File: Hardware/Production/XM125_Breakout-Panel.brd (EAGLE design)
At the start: 175 x 116.3 mm, 1266 parts, among them J104 SWD (DNP), J106 RIGHT_ANGLE, J107 RIGHT_ANGLE, J117 SWD (DNP), J119 RIGHT_ANGLE, J120 RIGHT_ANGLE, J13 SWD (DNP), J130 SWD (DNP), J132 RIGHT_ANGLE, J133 RIGHT_ANGLE, J143 SWD (DNP), J145 RIGHT_ANGLE, J146 RIGHT_ANGLE, J15 RIGHT_ANGLE, J156 SWD (DNP), J16 RIGHT_ANGLE, J2 RIGHT_ANGLE, J26 SWD (DNP), J28 RIGHT_ANGLE, J29 RIGHT_ANGLE, J3 RIGHT_ANGLE, J39 SWD (DNP), J41 RIGHT_ANGLE, J42 RIGHT_ANGLE, J52 SWD (DNP), J54 RIGHT_ANGLE, J55 RIGHT_ANGLE, J65 SWD (DNP), J67 RIGHT_ANGLE, J68 RIGHT_ANGLE, J78 SWD (DNP), J80 RIGHT_ANGLE, J81 RIGHT_ANGLE, J91 SWD (DNP), J93 RIGHT_ANGLE, J94 RIGHT_ANGLE, U1 XM125, U10 XM125, U11 CH340C, U12 ESD Diode, U13 RT9080-33GJ5, U14 RT9080-18GJ5, U15 XM125, U16 CH340C, U17 ESD Diode, U18 RT9080-33GJ5, U19 RT9080-18GJ5, U2 RT9080-33GJ5, U20 XM125, U21 CH340C, U22 ESD Diode, U23 RT9080-33GJ5, U24 RT9080-18GJ5, U25 XM125, U26 CH340C, U27 ESD Diode, U28 RT9080-33GJ5, U29 RT9080-18GJ5, U3 RT9080-18GJ5, U30 XM125, U31 CH340C, U32 ESD Diode, U33 RT9080-33GJ5, U34 RT9080-18GJ5, U35 XM125, U36 CH340C, U37 ESD Diode, U38 RT9080-33GJ5, U39 RT9080-18GJ5, U4 CH340C, U40 XM125, U41 CH340C, U42 ESD Diode, U43 RT9080-33GJ5, U44 RT9080-18GJ5, U45 XM125, U46 CH340C, U47 ESD Diode, U48 RT9080-33GJ5, U49 RT9080-18GJ5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

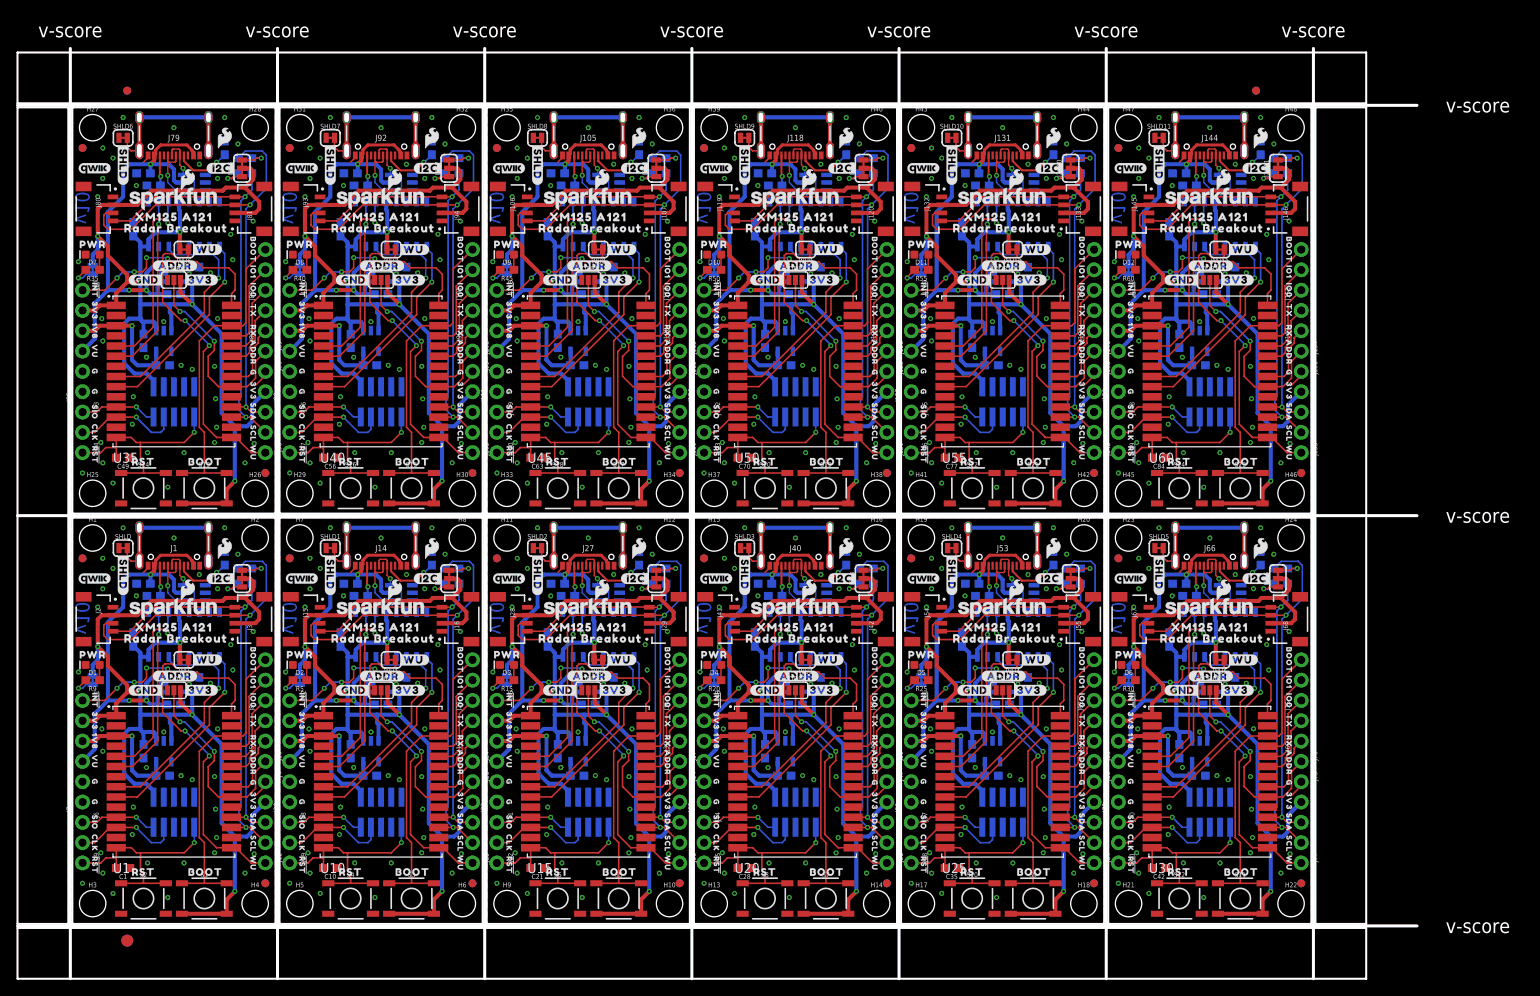
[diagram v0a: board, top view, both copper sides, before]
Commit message: Cleanup repo; design review changes
Check design review document for full list of changes/details.
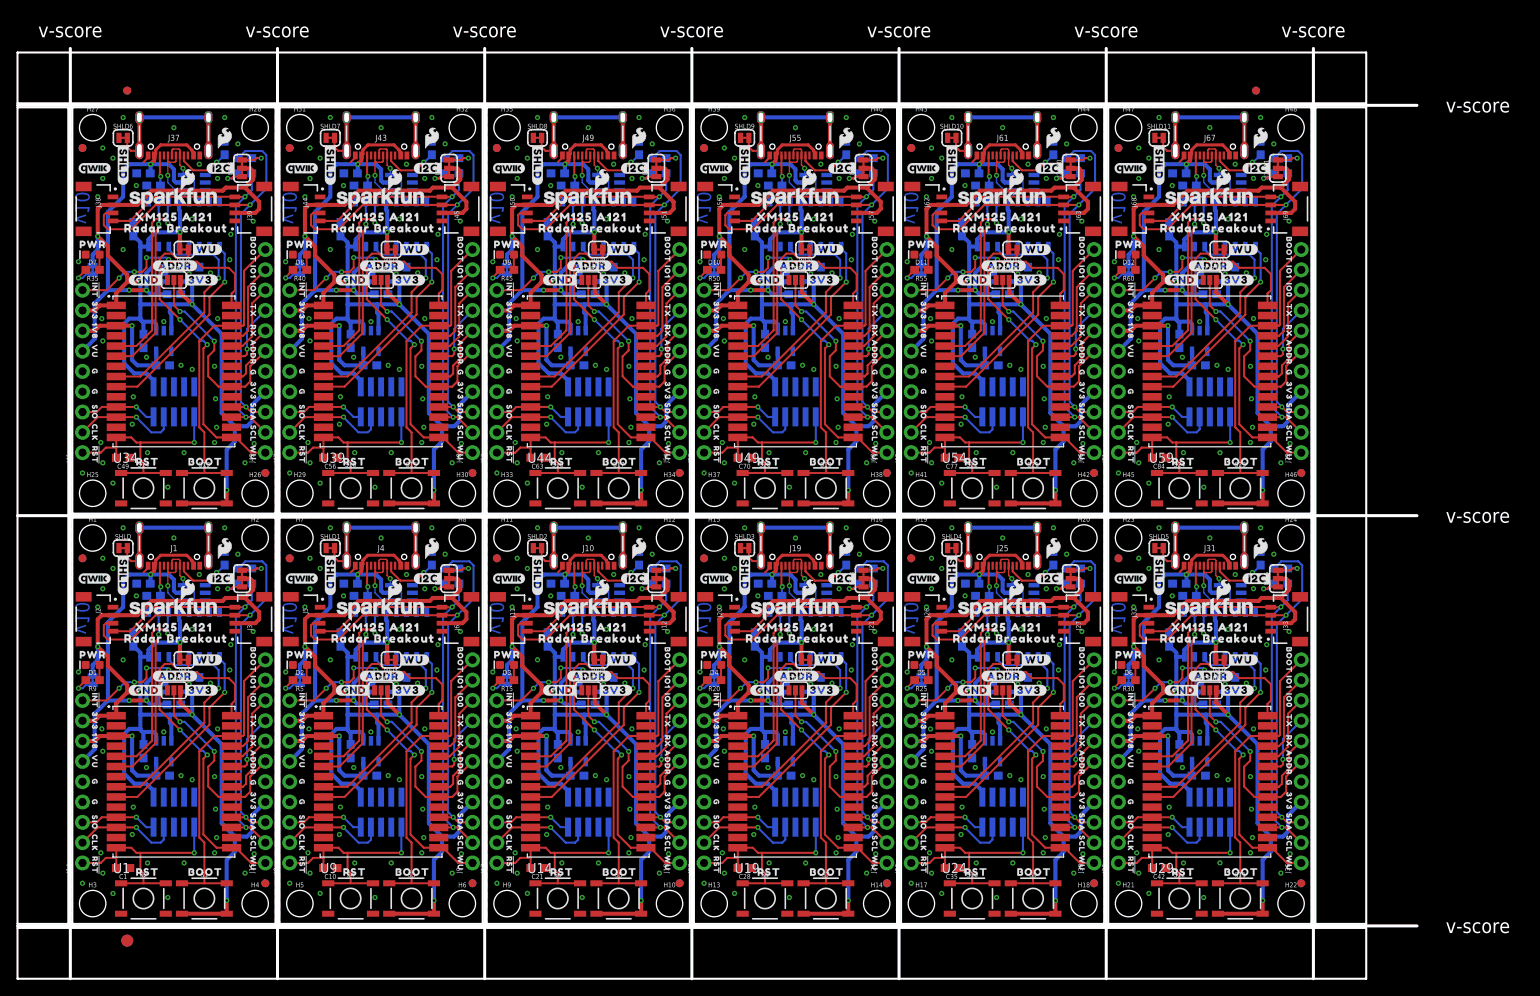
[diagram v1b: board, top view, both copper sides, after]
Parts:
- removed J100, J102, J103, J110, J113, J115, J116, J123, J126, J128, J129, J136, J139, J141, J142, J149, J152, J154, J155, J74, J76, J77, J84, J87, J89, J90, J97: (no value), SparkFun-Connectors:1X01_NO_SILK_STAND
- removed J101, J114, J127, J140, J153, J75, J88: (no value), SparkFun-Connectors:1X03_NO_SILK
- removed J104, J117, J130, J143, J156, J78, J91: SWD (DNP), SparkFun-Connectors:2X5-SMD-UNSHROUDED_DNP_NO_PASTE
- removed J105, J118, J131, J144, J79, J92: (no value), SparkFun-Connectors:USB-C-16P-2LAYER-PADS
- removed J106, J107, J119, J120, J132, J133, J145, J146, J80, J81, J93, J94: RIGHT_ANGLE, SparkFun-Connectors:JST04_1MM_RA
- removed J108, J109, J121, J122, J134, J135, J147, J148, J82, J83, J95, J96: (no value), SparkFun-Connectors:1X02_NO_SILK
- removed J111, J124, J137, J150, J85, J98: (no value), SparkFun-Connectors:1X05_NO_SILK
- removed J112, J125, J138, J151, J73, J86, J99: (no value), SparkFun-Connectors:1X04_NO_SILK
- J10, J19, J25, J37, J61: device SparkFun-Connectors:1X01_NO_SILK_STAND -> SparkFun-Connectors:USB-C-16P-2LAYER-PADS
- J11, J12, J32, J38, J45, J50, J51, J63: value (none) -> RIGHT_ANGLE; device SparkFun-Connectors:1X01_NO_SILK_STAND -> SparkFun-Connectors:JST04_1MM_RA
- J14, J53: device SparkFun-Connectors:USB-C-16P-2LAYER-PADS -> SparkFun-Connectors:1X09_NO_SILK
- J15, J42, J54: value RIGHT_ANGLE -> (none); device SparkFun-Connectors:JST04_1MM_RA -> SparkFun-Connectors:1X11_NO_SILK
- J16, J28: value RIGHT_ANGLE -> SWD (DNP); device SparkFun-Connectors:JST04_1MM_RA -> SparkFun-Connectors:2X5-SMD-UNSHROUDED_DNP_NO_PASTE
- J17: device SparkFun-Connectors:1X02_NO_SILK -> SparkFun-Connectors:1X09_NO_SILK
- J18, J30: device SparkFun-Connectors:1X02_NO_SILK -> SparkFun-Connectors:1X11_NO_SILK
- J20, J33: value (none) -> RIGHT_ANGLE; device SparkFun-Connectors:1X05_NO_SILK -> SparkFun-Connectors:JST04_1MM_RA
- J21: value (none) -> RIGHT_ANGLE; device SparkFun-Connectors:1X04_NO_SILK -> SparkFun-Connectors:JST04_1MM_RA
- J22, J58, J64: value (none) -> SWD (DNP); device SparkFun-Connectors:1X01_NO_SILK_STAND -> SparkFun-Connectors:2X5-SMD-UNSHROUDED_DNP_NO_PASTE
- J23, J8: device SparkFun-Connectors:1X03_NO_SILK -> SparkFun-Connectors:1X09_NO_SILK
- J24, J48, J9: device SparkFun-Connectors:1X01_NO_SILK_STAND -> SparkFun-Connectors:1X11_NO_SILK
- J26, J39: value SWD (DNP) -> RIGHT_ANGLE; device SparkFun-Connectors:2X5-SMD-UNSHROUDED_DNP_NO_PASTE -> SparkFun-Connectors:JST04_1MM_RA
- J27: value (none) -> RIGHT_ANGLE; device SparkFun-Connectors:USB-C-16P-2LAYER-PADS -> SparkFun-Connectors:JST04_1MM_RA
- J29, J41: value RIGHT_ANGLE -> (none); device SparkFun-Connectors:JST04_1MM_RA -> SparkFun-Connectors:1X09_NO_SILK
- J31, J43: device SparkFun-Connectors:1X02_NO_SILK -> SparkFun-Connectors:USB-C-16P-2LAYER-PADS
- J34: value (none) -> SWD (DNP); device SparkFun-Connectors:1X04_NO_SILK -> SparkFun-Connectors:2X5-SMD-UNSHROUDED_DNP_NO_PASTE
- J35, J71: device SparkFun-Connectors:1X01_NO_SILK_STAND -> SparkFun-Connectors:1X09_NO_SILK
- J36: device SparkFun-Connectors:1X03_NO_SILK -> SparkFun-Connectors:1X11_NO_SILK
- J4: device SparkFun-Connectors:1X04_NO_SILK -> SparkFun-Connectors:USB-C-16P-2LAYER-PADS
- J40: value (none) -> SWD (DNP); device SparkFun-Connectors:USB-C-16P-2LAYER-PADS -> SparkFun-Connectors:2X5-SMD-UNSHROUDED_DNP_NO_PASTE
- J44, J5, J56, J57, J6, J69: value (none) -> RIGHT_ANGLE; device SparkFun-Connectors:1X02_NO_SILK -> SparkFun-Connectors:JST04_1MM_RA
- J46, J7: value (none) -> SWD (DNP); device SparkFun-Connectors:1X05_NO_SILK -> SparkFun-Connectors:2X5-SMD-UNSHROUDED_DNP_NO_PASTE
- J47: device SparkFun-Connectors:1X04_NO_SILK -> SparkFun-Connectors:1X09_NO_SILK
- J49: device SparkFun-Connectors:1X03_NO_SILK -> SparkFun-Connectors:USB-C-16P-2LAYER-PADS
- J55, J67: value RIGHT_ANGLE -> (none); device SparkFun-Connectors:JST04_1MM_RA -> SparkFun-Connectors:USB-C-16P-2LAYER-PADS
- J59: device SparkFun-Connectors:1X05_NO_SILK -> SparkFun-Connectors:1X09_NO_SILK
- J60: device SparkFun-Connectors:1X04_NO_SILK -> SparkFun-Connectors:1X11_NO_SILK
- J62: value (none) -> RIGHT_ANGLE; device SparkFun-Connectors:1X03_NO_SILK -> SparkFun-Connectors:JST04_1MM_RA
- J65: value SWD (DNP) -> (none); device SparkFun-Connectors:2X5-SMD-UNSHROUDED_DNP_NO_PASTE -> SparkFun-Connectors:1X09_NO_SILK
- J66: device SparkFun-Connectors:USB-C-16P-2LAYER-PADS -> SparkFun-Connectors:1X11_NO_SILK
- J70: value (none) -> SWD (DNP); device SparkFun-Connectors:1X02_NO_SILK -> SparkFun-Connectors:2X5-SMD-UNSHROUDED_DNP_NO_PASTE
- J72: device SparkFun-Connectors:1X05_NO_SILK -> SparkFun-Connectors:1X11_NO_SILK
- U10, U15, U20, U25, U30, U35, U40, U45, U50, U55, U60: value XM125 -> ESD Diode; device XM125:XM125_ACC -> SparkFun-DiscreteSemi:SOT-23-6
- U12, U17, U22, U27, U32, U37, U42, U47, U52, U57, U7: value ESD Diode -> RT9080-33GJ5; device SparkFun-DiscreteSemi:SOT-23-6 -> SparkFun-IC-Power:SOT23-5
- U13, U18, U23, U28, U33, U38, U43, U48, U53, U58, U8: value RT9080-33GJ5 -> RT9080-18GJ5; device SparkFun-IC-Power:SOT23-5 -> XM125:SOT23-5
- U14, U19, U24, U29, U34, U39, U44, U49, U54, U59, U9: value RT9080-18GJ5 -> XM125; device XM125:SOT23-5 -> XM125:XM125_ACC
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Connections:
- removed net N$100: J144.A6, J144.B6, U56.5, U57.4
- removed net N$19 (its old number): J27.A6, J27.B6, U11.5, U12.4
- removed net N$20: J27.A7, J27.B7, U11.6, U12.6
- removed net N$28 (its old number): J40.A6, J40.B6, U16.5, U17.4
- removed net N$29 (its old number): J40.A7, J40.B7, U16.6, U17.6
- removed net N$3: J14.A6, J14.B6, U6.5, U7.4
- removed net N$30: J40.SHLD1, J40.SHLD2, J40.SHLD3, J40.SHLD4, SHLD3.2
- removed net N$37 (its old number): J53.A6, J53.B6, U21.5, U22.4
- removed net N$38 (its old number): J53.A7, J53.B7, U21.6, U22.6
- removed net N$39 (its old number): J53.SHLD1, J53.SHLD2, J53.SHLD3, J53.SHLD4, SHLD4.2
- removed net N$40: J53.B5, R22.2
- removed net N$46 (its old number): J66.A6, J66.B6, U26.5, U27.4
- removed net N$47 (its old number): J66.A7, J66.B7, U26.6, U27.6
- removed net N$48 (its old number): J66.SHLD1, J66.SHLD2, J66.SHLD3, J66.SHLD4, SHLD5.2
- removed net N$49 (its old number): J66.B5, R27.2
- removed net N$50: J66.A5, R26.2
- removed net N$56 (its old number): J79.A7, J79.B7, U31.6, U32.6
- removed net N$57 (its old number): J79.SHLD1, J79.SHLD2, J79.SHLD3, J79.SHLD4, SHLD6.2
- removed net N$58 (its old number): J79.B5, R32.2
- removed net N$59 (its old number): J79.A5, R31.2
- removed net N$66 (its old number): J92.SHLD1, J92.SHLD2, J92.SHLD3, J92.SHLD4, SHLD7.2
- removed net N$67 (its old number): J92.B5, R37.2
- removed net N$68 (its old number): J92.A5, R36.2
- removed net N$76 (its old number): J105.B5, R42.2
- removed net N$77 (its old number): J105.A5, R41.2
- removed net N$86 (its old number): J118.A5, R46.2
- new net N$105: J61.A5, R51.2
- new net N$111: J67.A6, J67.B6, U56.5, U60.4
- new net N$112: J67.A7, J67.B7, U56.6, U60.6
- new net N$113: J67.SHLD1, J67.SHLD2, J67.SHLD3, J67.SHLD4, SHLD11.2
- new net N$114: J67.B5, R57.2
- new net N$115: J67.A5, R56.2
- new net N$24: J10.B5, R10.2
- new net N$25: J10.A5, R6.2
- new net N$33: J19.SHLD1, J19.SHLD2, J19.SHLD3, J19.SHLD4, SHLD3.2
- new net N$34: J19.B5, R17.2
- new net N$35: J19.A5, R16.2
- new net N$42: J25.A7, J25.B7, U21.6, U25.6
- new net N$43: J25.SHLD1, J25.SHLD2, J25.SHLD3, J25.SHLD4, SHLD4.2
- new net N$44: J25.B5, R22.2
- new net N$45: J25.A5, R21.2
- new net N$51: J31.A6, J31.B6, U26.5, U30.4
- new net N$52: J31.A7, J31.B7, U26.6, U30.6
- new net N$53: J31.SHLD1, J31.SHLD2, J31.SHLD3, J31.SHLD4, SHLD5.2
- new net N$54: J31.B5, R27.2
- new net N$61: J37.A6, J37.B6, U31.5, U35.4
- new net N$62: J37.A7, J37.B7, U31.6, U35.6
- new net N$63: J37.SHLD1, J37.SHLD2, J37.SHLD3, J37.SHLD4, SHLD6.2
- new net N$71: J43.A6, J43.B6, U36.5, U40.4
- new net N$72: J43.A7, J43.B7, U36.6, U40.6
- new net N$8: J4.A5, R1.2
- new net N$81: J49.A6, J49.B6, U41.5, U45.4
- net !XM125_INT: now also J14.9; no longer J11.1
- net !XM125_INT1: now also J8.9, U9.28; no longer J22.1, U10.28
- net !XM125_INT10: now also J65.9, U54.28; no longer J139.1, U55.28
- net !XM125_INT11: now also J71.9, U59.28; no longer J152.1, U60.28
- net !XM125_INT2: now also J17.9, U14.28; no longer J35.1, U15.28
- net !XM125_INT3: now also J23.9, U19.28; no longer J48.1, U20.28
- net !XM125_INT4: now also J29.9, U24.28; no longer J61.1, U25.28
- net !XM125_INT5: now also J35.9, U29.28; no longer J74.1, U30.28
- net !XM125_INT6: now also J41.9, U34.28; no longer J87.1, U35.28
- net !XM125_INT7: now also J47.9, U39.28; no longer J100.1, U40.28
- net !XM125_INT8: now also J53.9, U44.28; no longer J113.1, U45.28
- net !XM125_INT9: now also J59.9, U49.28; no longer J126.1, U50.28
- net !XM125_RESET: now also J14.1; no longer J9.1
- net !XM125_RESET1: now also J7.10, J8.1, U9.14; no longer J19.1, J26.10, U10.14
- net !XM125_RESET10: now also J64.10, J65.1, U54.14; no longer J136.1, J143.10, U55.14
- net !XM125_RESET11: now also J70.10, J71.1, U59.14; no longer J149.1, J156.10, U60.14
- net !XM125_RESET2: now also J16.10, J17.1, U14.14; no longer J32.1, J39.10, U15.14
- net !XM125_RESET3: now also J22.10, J23.1, U19.14; no longer J45.1, J52.10, U20.14
- net !XM125_RESET4: now also J28.10, J29.1, U24.14; no longer J58.1, J65.10, U25.14
- net !XM125_RESET5: now also J34.10, J35.1, U29.14; no longer J71.1, J78.10, U30.14
- net !XM125_RESET6: now also J40.10, J41.1, U34.14; no longer J84.1, J91.10, U35.14
- net !XM125_RESET7: now also J46.10, J47.1, U39.14; no longer J104.10, J97.1, U40.14
- net !XM125_RESET8: now also J52.10, J53.1, U44.14; no longer J110.1, J117.10, U45.14
- net !XM125_RESET9: now also J58.10, J59.1, U49.14; no longer J123.1, J130.10, U50.14
- net 1.8V: now also J14.7; no longer J7.4
- net 1.8V1: now also J8.7, U8.5, U9.3; no longer J20.4, U10.3, U9.5
- net 1.8V10: now also J65.7, U53.5, U54.3; no longer J137.4, U54.5, U55.3
- net 1.8V11: now also J71.7, U58.5, U59.3; no longer J150.4, U59.5, U60.3
- net 1.8V2: now also J17.7, U13.5, U14.3; no longer J33.4, U14.5, U15.3
- net 1.8V3: now also J23.7, U18.5, U19.3; no longer J46.4, U19.5, U20.3
- net 1.8V4: now also J29.7, U23.5, U24.3; no longer J59.4, U24.5, U25.3
- net 1.8V5: now also J35.7, U28.5, U29.3; no longer J72.4, U29.5, U30.3
- net 1.8V6: now also J41.7, U33.5, U34.3; no longer J85.4, U34.5, U35.3
- net 1.8V7: now also J47.7, U38.5, U39.3; no longer J98.4, U39.5, U40.3
- net 1.8V8: now also J53.7, U43.5, U44.3; no longer J111.4, U44.5, U45.3
- net 1.8V9: now also J59.7, U48.5, U49.3; no longer J124.4, U49.5, U50.3
- net 3.3V: now also J14.8, J15.4; no longer J4.2, J7.5
- net 3.3V1: now also J5.2, J6.2, J7.1, J8.8, J9.4, U7.5, U8.1, U8.3; no longer J15.2, J16.2, J20.5, J21.2, J26.1, U10.1, U8.5, U9.3
- net 3.3V10: now also J62.2, J63.2, J64.1, J65.8, J66.4, U52.5, U53.1, U53.3; no longer J132.2, J133.2, J137.5, J138.2, J143.1, U53.5, U54.3, U55.1
- net 3.3V11: now also J68.2, J69.2, J70.1, J71.8, J72.4, U57.5, U58.1, U58.3; no longer J145.2, J146.2, J150.5, J151.2, J156.1, U58.5, U59.3, U60.1
- net 3.3V2: now also J11.2, J12.2, J16.1, J17.8, J18.4, U12.5, U13.1, U13.3; no longer J28.2, J29.2, J33.5, J34.2, J39.1, U13.5, U14.3, U15.1
- net 3.3V3: now also J20.2, J21.2, J22.1, J23.8, J24.4, U17.5, U18.1, U18.3; no longer J41.2, J42.2, J46.5, J47.2, J52.1, U18.5, U19.3, U20.1
- net 3.3V4: now also J26.2, J27.2, J28.1, J29.8, J30.4, U22.5, U23.1, U23.3; no longer J54.2, J55.2, J59.5, J60.2, J65.1, U23.5, U24.3, U25.1
- net 3.3V5: now also J32.2, J33.2, J34.1, J35.8, J36.4, U27.5, U28.1, U28.3; no longer J67.2, J68.2, J72.5, J73.2, J78.1, U28.5, U29.3, U30.1
- net 3.3V6: now also J38.2, J39.2, J40.1, J41.8, J42.4, U32.5, U33.1, U33.3; no longer J80.2, J81.2, J85.5, J86.2, J91.1, U33.5, U34.3, U35.1
- net 3.3V7: now also J44.2, J45.2, J46.1, J47.8, J48.4, U37.5, U38.1, U38.3; no longer J104.1, J93.2, J94.2, J98.5, J99.2, U38.5, U39.3, U40.1
- net 3.3V8: now also J50.2, J51.2, J52.1, J53.8, J54.4, U42.5, U43.1, U43.3; no longer J106.2, J107.2, J111.5, J112.2, J117.1, U43.5, U44.3, U45.1
- net 3.3V9: now also J56.2, J57.2, J58.1, J59.8, J60.4, U47.5, U48.1, U48.3; no longer J119.2, J120.2, J124.5, J125.2, J130.1, U48.5, U49.3, U50.1
- net CH340-CTS1: now also U9.9; no longer U10.9
- net CH340-CTS10: now also U54.9; no longer U55.9
- net CH340-CTS11: now also U59.9; no longer U60.9
- net CH340-CTS2: now also U14.9; no longer U15.9
- net CH340-CTS3: now also U19.9; no longer U20.9
- net CH340-CTS4: now also U24.9; no longer U25.9
- net CH340-CTS5: now also U29.9; no longer U30.9
- net CH340-CTS6: now also U34.9; no longer U35.9
- net CH340-CTS7: now also U39.9; no longer U40.9
- net CH340-CTS8: now also U44.9; no longer U45.9
- net CH340-CTS9: now also U49.9; no longer U50.9
- net CH340-RTS1: now also U9.8; no longer U10.8
- net CH340-RTS10: now also U54.8; no longer U55.8
- net CH340-RTS11: now also U59.8; no longer U60.8
- net CH340-RTS2: now also U14.8; no longer U15.8
- net CH340-RTS3: now also U19.8; no longer U20.8
- net CH340-RTS4: now also U24.8; no longer U25.8
- net CH340-RTS5: now also U29.8; no longer U30.8
- net CH340-RTS6: now also U34.8; no longer U35.8
- net CH340-RTS7: now also U39.8; no longer U40.8
- net CH340-RTS8: now also U44.8; no longer U45.8
- net CH340-RTS9: now also U49.8; no longer U50.8
- net CH340-RX1: now also U9.5; no longer U10.5
- net CH340-RX10: now also U54.5; no longer U55.5
- net CH340-RX11: now also U59.5; no longer U60.5
- net CH340-RX2: now also U14.5; no longer U15.5
- net CH340-RX3: now also U19.5; no longer U20.5
- net CH340-RX4: now also U24.5; no longer U25.5
- net CH340-RX5: now also U29.5; no longer U30.5
- net CH340-RX6: now also U34.5; no longer U35.5
- net CH340-RX7: now also U39.5; no longer U40.5
- net CH340-RX8: now also U44.5; no longer U45.5
- net CH340-RX9: now also U49.5; no longer U50.5
- net CH340-TX1: now also U9.6; no longer U10.6
- net CH340-TX10: now also U54.6; no longer U55.6
- net CH340-TX11: now also U59.6; no longer U60.6
- net CH340-TX2: now also U14.6; no longer U15.6
- net CH340-TX3: now also U19.6; no longer U20.6
- net CH340-TX4: now also U24.6; no longer U25.6
- net CH340-TX5: now also U29.6; no longer U30.6
- net CH340-TX6: now also U34.6; no longer U35.6
- net CH340-TX7: now also U39.6; no longer U40.6
- net CH340-TX8: now also U44.6; no longer U45.6
- net CH340-TX9: now also U49.6; no longer U50.6
- net DEBUG_UART-RX: now also J15.7; no longer J5.1
- net DEBUG_UART-RX1: now also J9.7, U9.21; no longer J17.1, U10.21
- net DEBUG_UART-RX10: now also J66.7, U54.21; no longer J134.1, U55.21
- net DEBUG_UART-RX11: now also J72.7, U59.21; no longer J147.1, U60.21
- net DEBUG_UART-RX2: now also J18.7, U14.21; no longer J30.1, U15.21
- net DEBUG_UART-RX3: now also J24.7, U19.21; no longer J43.1, U20.21
- net DEBUG_UART-RX4: now also J30.7, U24.21; no longer J56.1, U25.21
- net DEBUG_UART-RX5: now also J36.7, U29.21; no longer J69.1, U30.21
- net DEBUG_UART-RX6: now also J42.7, U34.21; no longer J82.1, U35.21
- net DEBUG_UART-RX7: now also J48.7, U39.21; no longer J95.1, U40.21
- net DEBUG_UART-RX8: now also J54.7, U44.21; no longer J108.1, U45.21
- net DEBUG_UART-RX9: now also J60.7, U49.21; no longer J121.1, U50.21
- net DEBUG_UART-TX: now also J15.8; no longer J5.2
- net DEBUG_UART-TX1: now also J9.8, U9.23; no longer J17.2, U10.23
- net DEBUG_UART-TX10: now also J66.8, U54.23; no longer J134.2, U55.23
- net DEBUG_UART-TX11: now also J72.8, U59.23; no longer J147.2, U60.23
- net DEBUG_UART-TX2: now also J18.8, U14.23; no longer J30.2, U15.23
- net DEBUG_UART-TX3: now also J24.8, U19.23; no longer J43.2, U20.23
- net DEBUG_UART-TX4: now also J30.8, U24.23; no longer J56.2, U25.23
- net DEBUG_UART-TX5: now also J36.8, U29.23; no longer J69.2, U30.23
- net DEBUG_UART-TX6: now also J42.8, U34.23; no longer J82.2, U35.23
- net DEBUG_UART-TX7: now also J48.8, U39.23; no longer J95.2, U40.23
- net DEBUG_UART-TX8: now also J54.8, U44.23; no longer J108.2, U45.23
- net DEBUG_UART-TX9: now also J60.8, U49.23; no longer J121.2, U50.23
- net GND: now also J14.4, J14.5, J15.5; no longer J4.1, J7.1, J7.2
- net GND1: now also J4.GND, J4.GND2, J5.1, J6.1, J7.3, J7.5, J7.9, J8.4, J8.5, J9.5, U9.10, U9.13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; no longer J14.GND, J14.GND2, J15.1, J16.1, J20.1, J20.2, J21.1, J26.3, J26.5, J26.9, U10.10, U10.13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
- net GND10: now also J61.GND, J61.GND2, J62.1, J63.1, J64.3, J64.5, J64.9, J65.4, J65.5, J66.5, U54.10, U54.13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; no longer J131.GND, J131.GND2, J132.1, J133.1, J137.1, J137.2, J138.1, J143.3, J143.5, J143.9, U55.10, U55.13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
- net GND11: now also J67.GND, J67.GND2, J68.1, J69.1, J70.3, J70.5, J70.9, J71.4, J71.5, J72.5, U59.10, U59.13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; no longer J144.GND, J144.GND2, J145.1, J146.1, J150.1, J150.2, J151.1, J156.3, J156.5, J156.9, U60.10, U60.13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
- net GND2: now also J10.GND, J10.GND2, J11.1, J12.1, J16.3, J16.5, J16.9, J17.4, J17.5, J18.5, U14.10, U14.13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; no longer J27.GND, J27.GND2, J28.1, J29.1, J33.1, J33.2, J34.1, J39.3, J39.5, J39.9, U15.10, U15.13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
- net GND3: now also J19.GND, J19.GND2, J20.1, J21.1, J22.3, J22.5, J22.9, J23.4, J23.5, J24.5, U19.10, U19.13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; no longer J40.GND, J40.GND2, J41.1, J42.1, J46.1, J46.2, J47.1, J52.3, J52.5, J52.9, U20.10, U20.13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
- net GND4: now also J25.GND, J25.GND2, J26.1, J27.1, J28.3, J28.5, J28.9, J29.4, J29.5, J30.5, U24.10, U24.13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; no longer J53.GND, J53.GND2, J54.1, J55.1, J59.1, J59.2, J60.1, J65.3, J65.5, J65.9, U25.10, U25.13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
- net GND5: now also J31.GND, J31.GND2, J32.1, J33.1, J34.3, J34.5, J34.9, J35.4, J35.5, J36.5, U29.10, U29.13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; no longer J66.GND, J66.GND2, J67.1, J68.1, J72.1, J72.2, J73.1, J78.3, J78.5, J78.9, U30.10, U30.13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
- net GND6: now also J37.GND, J37.GND2, J38.1, J39.1, J40.3, J40.5, J40.9, J41.4, J41.5, J42.5, U34.10, U34.13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; no longer J79.GND, J79.GND2, J80.1, J81.1, J85.1, J85.2, J86.1, J91.3, J91.5, J91.9, U35.10, U35.13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
- net GND7: now also J43.GND, J43.GND2, J44.1, J45.1, J46.3, J46.5, J46.9, J47.4, J47.5, J48.5, U39.10, U39.13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; no longer J104.3, J104.5, J104.9, J92.GND, J92.GND2, J93.1, J94.1, J98.1, J98.2, J99.1, U40.10, U40.13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
- net GND8: now also J49.GND, J49.GND2, J50.1, J51.1, J52.3, J52.5, J52.9, J53.4, J53.5, J54.5, U44.10, U44.13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; no longer J105.GND, J105.GND2, J106.1, J107.1, J111.1, J111.2, J112.1, J117.3, J117.5, J117.9, U45.10, U45.13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
- net GND9: now also J55.GND, J55.GND2, J56.1, J57.1, J58.3, J58.5, J58.9, J59.4, J59.5, J60.5, U49.10, U49.13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; no longer J118.GND, J118.GND2, J119.1, J120.1, J124.1, J124.2, J125.1, J130.3, J130.5, J130.9, U50.10, U50.13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
- net N$101: now also J61.A6, J61.B6, U51.5, U55.4; no longer J144.A7, J144.B7, U56.6, U57.6
- net N$102: now also J61.A7, J61.B7, U51.6, U55.6; no longer J144.SHLD1, J144.SHLD2, J144.SHLD3, J144.SHLD4, SHLD11.2
- net N$103: now also J61.SHLD1, J61.SHLD2, J61.SHLD3, J61.SHLD4, SHLD10.2; no longer J144.B5, R57.2
- net N$104: now also J61.B5, R52.2; no longer J144.A5, R56.2
- net N$21: now also J10.A6, J10.B6, U11.5, U15.4; no longer J27.SHLD1, J27.SHLD2, J27.SHLD3, J27.SHLD4, SHLD2.2
- net N$22: now also J10.A7, J10.B7, U11.6, U15.6; no longer J27.B5, R10.2
- net N$23: now also J10.SHLD1, J10.SHLD2, J10.SHLD3, J10.SHLD4, SHLD2.2; no longer J27.A5, R6.2
- net N$31: now also J19.A6, J19.B6, U16.5, U20.4; no longer J40.B5, R17.2
- net N$32: now also J19.A7, J19.B7, U16.6, U20.6; no longer J40.A5, R16.2
- net N$4: now also J4.A6, J4.B6, U10.4, U6.5; no longer J14.A7, J14.B7, U6.6, U7.6
- net N$41: now also J25.A6, J25.B6, U21.5, U25.4; no longer J53.A5, R21.2
- net N$5: now also J4.A7, J4.B7, U10.6, U6.6; no longer J14.SHLD1, J14.SHLD2, J14.SHLD3, J14.SHLD4, SHLD1.2
- net N$55: now also J31.A5, R26.2; no longer J79.A6, J79.B6, U31.5, U32.4
- net N$6: now also J4.SHLD1, J4.SHLD2, J4.SHLD3, J4.SHLD4, SHLD1.2; no longer J14.B5, R2.2
- net N$64: now also J37.B5, R32.2; no longer J92.A6, J92.B6, U36.5, U37.4
- net N$65: now also J37.A5, R31.2; no longer J92.A7, J92.B7, U36.6, U37.6
- net N$7: now also J4.B5, R2.2; no longer J14.A5, R1.2
- net N$73: now also J43.SHLD1, J43.SHLD2, J43.SHLD3, J43.SHLD4, SHLD7.2; no longer J105.A6, J105.B6, U41.5, U42.4
- net N$74: now also J43.B5, R37.2; no longer J105.A7, J105.B7, U41.6, U42.6
- net N$75: now also J43.A5, R36.2; no longer J105.SHLD1, J105.SHLD2, J105.SHLD3, J105.SHLD4, SHLD8.2
- net N$82: now also J49.A7, J49.B7, U41.6, U45.6; no longer J118.A6, J118.B6, U46.5, U47.4
- net N$83: now also J49.SHLD1, J49.SHLD2, J49.SHLD3, J49.SHLD4, SHLD8.2; no longer J118.A7, J118.B7, U46.6, U47.6
- net N$84: now also J49.B5, R42.2; no longer J118.SHLD1, J118.SHLD2, J118.SHLD3, J118.SHLD4, SHLD9.2
- net N$85: now also J49.A5, R41.2; no longer J118.B5, R47.2
- net N$91: now also J55.A6, J55.B6, U46.5, U50.4; no longer J131.A6, J131.B6, U51.5, U52.4
- net N$92: now also J55.A7, J55.B7, U46.6, U50.6; no longer J131.A7, J131.B7, U51.6, U52.6
- net N$93: now also J55.SHLD1, J55.SHLD2, J55.SHLD3, J55.SHLD4, SHLD9.2; no longer J131.SHLD1, J131.SHLD2, J131.SHLD3, J131.SHLD4, SHLD10.2
- net N$94: now also J55.B5, R47.2; no longer J131.B5, R52.2
- net N$95: now also J55.A5, R46.2; no longer J131.A5, R51.2
- net SCL: now also J15.2; no longer J4.4
- net SCL1: now also J5.4, J6.4, J9.2, U9.17; no longer J15.4, J16.4, J21.4, U10.17
- net SCL10: now also J62.4, J63.4, J66.2, U54.17; no longer J132.4, J133.4, J138.4, U55.17
- net SCL11: now also J68.4, J69.4, J72.2, U59.17; no longer J145.4, J146.4, J151.4, U60.17
- net SCL2: now also J11.4, J12.4, J18.2, U14.17; no longer J28.4, J29.4, J34.4, U15.17
- net SCL3: now also J20.4, J21.4, J24.2, U19.17; no longer J41.4, J42.4, J47.4, U20.17
- net SCL4: now also J26.4, J27.4, J30.2, U24.17; no longer J54.4, J55.4, J60.4, U25.17
- net SCL5: now also J32.4, J33.4, J36.2, U29.17; no longer J67.4, J68.4, J73.4, U30.17
- net SCL6: now also J38.4, J39.4, J42.2, U34.17; no longer J80.4, J81.4, J86.4, U35.17
- net SCL7: now also J44.4, J45.4, J48.2, U39.17; no longer J93.4, J94.4, J99.4, U40.17
- net SCL8: now also J50.4, J51.4, J54.2, U44.17; no longer J106.4, J107.4, J112.4, U45.17
- net SCL9: now also J56.4, J57.4, J60.2, U49.17; no longer J119.4, J120.4, J125.4, U50.17
- net SDA: now also J15.3; no longer J4.3
- net SDA1: now also J5.3, J6.3, J9.3, U9.18; no longer J15.3, J16.3, J21.3, U10.18
- net SDA10: now also J62.3, J63.3, J66.3, U54.18; no longer J132.3, J133.3, J138.3, U55.18
- net SDA11: now also J68.3, J69.3, J72.3, U59.18; no longer J145.3, J146.3, J151.3, U60.18
- net SDA2: now also J11.3, J12.3, J18.3, U14.18; no longer J28.3, J29.3, J34.3, U15.18
- net SDA3: now also J20.3, J21.3, J24.3, U19.18; no longer J41.3, J42.3, J47.3, U20.18
- net SDA4: now also J26.3, J27.3, J30.3, U24.18; no longer J54.3, J55.3, J60.3, U25.18
- net SDA5: now also J32.3, J33.3, J36.3, U29.18; no longer J67.3, J68.3, J73.3, U30.18
- net SDA6: now also J38.3, J39.3, J42.3, U34.18; no longer J80.3, J81.3, J86.3, U35.18
- net SDA7: now also J44.3, J45.3, J48.3, U39.18; no longer J93.3, J94.3, J99.3, U40.18
- net SDA8: now also J50.3, J51.3, J54.3, U44.18; no longer J106.3, J107.3, J112.3, U45.18
- net SDA9: now also J56.3, J57.3, J60.3, U49.18; no longer J119.3, J120.3, J125.3, U50.18
- net SWD_CLK: now also J14.2; no longer J6.2
- net SWD_CLK1: now also J7.4, J8.2, U9.12; no longer J18.2, J26.4, U10.12
- net SWD_CLK10: now also J64.4, J65.2, U54.12; no longer J135.2, J143.4, U55.12
- net SWD_CLK11: now also J70.4, J71.2, U59.12; no longer J148.2, J156.4, U60.12
- net SWD_CLK2: now also J16.4, J17.2, U14.12; no longer J31.2, J39.4, U15.12
- net SWD_CLK3: now also J22.4, J23.2, U19.12; no longer J44.2, J52.4, U20.12
- net SWD_CLK4: now also J28.4, J29.2, U24.12; no longer J57.2, J65.4, U25.12
- net SWD_CLK5: now also J34.4, J35.2, U29.12; no longer J70.2, J78.4, U30.12
- net SWD_CLK6: now also J40.4, J41.2, U34.12; no longer J83.2, J91.4, U35.12
- net SWD_CLK7: now also J46.4, J47.2, U39.12; no longer J104.4, J96.2, U40.12
- net SWD_CLK8: now also J52.4, J53.2, U44.12; no longer J109.2, J117.4, U45.12
- net SWD_CLK9: now also J58.4, J59.2, U49.12; no longer J122.2, J130.4, U50.12
- net SWD_IO: now also J14.3; no longer J6.1
- net SWD_IO1: now also J7.2, J8.3, U9.11; no longer J18.1, J26.2, U10.11
- net SWD_IO10: now also J64.2, J65.3, U54.11; no longer J135.1, J143.2, U55.11
- net SWD_IO11: now also J70.2, J71.3, U59.11; no longer J148.1, J156.2, U60.11
- net SWD_IO2: now also J16.2, J17.3, U14.11; no longer J31.1, J39.2, U15.11
- net SWD_IO3: now also J22.2, J23.3, U19.11; no longer J44.1, J52.2, U20.11
- net SWD_IO4: now also J28.2, J29.3, U24.11; no longer J57.1, J65.2, U25.11
- net SWD_IO5: now also J34.2, J35.3, U29.11; no longer J70.1, J78.2, U30.11
- net SWD_IO6: now also J40.2, J41.3, U34.11; no longer J83.1, J91.2, U35.11
- net SWD_IO7: now also J46.2, J47.3, U39.11; no longer J104.2, J96.1, U40.11
- net SWD_IO8: now also J52.2, J53.3, U44.11; no longer J109.1, J117.2, U45.11
- net SWD_IO9: now also J58.2, J59.3, U49.11; no longer J122.1, J130.2, U50.11
- net V_USB: now also J14.6; no longer J7.3
- net V_USB1: now also J4.VBUS1, J4.VBUS2, J8.6, U10.5, U7.1, U7.3; no longer J14.VBUS1, J14.VBUS2, J20.3, U7.5, U8.1, U8.3
- net V_USB10: now also J61.VBUS1, J61.VBUS2, J65.6, U52.1, U52.3, U55.5; no longer J131.VBUS1, J131.VBUS2, J137.3, U52.5, U53.1, U53.3
- net V_USB11: now also J67.VBUS1, J67.VBUS2, J71.6, U57.1, U57.3, U60.5; no longer J144.VBUS1, J144.VBUS2, J150.3, U57.5, U58.1, U58.3
- net V_USB2: now also J10.VBUS1, J10.VBUS2, J17.6, U12.1, U12.3, U15.5; no longer J27.VBUS1, J27.VBUS2, J33.3, U12.5, U13.1, U13.3
- net V_USB3: now also J19.VBUS1, J19.VBUS2, J23.6, U17.1, U17.3, U20.5; no longer J40.VBUS1, J40.VBUS2, J46.3, U17.5, U18.1, U18.3
- net V_USB4: now also J25.VBUS1, J25.VBUS2, J29.6, U22.1, U22.3, U25.5; no longer J53.VBUS1, J53.VBUS2, J59.3, U22.5, U23.1, U23.3
- net V_USB5: now also J31.VBUS1, J31.VBUS2, J35.6, U27.1, U27.3, U30.5; no longer J66.VBUS1, J66.VBUS2, J72.3, U27.5, U28.1, U28.3
- net V_USB6: now also J37.VBUS1, J37.VBUS2, J41.6, U32.1, U32.3, U35.5; no longer J79.VBUS1, J79.VBUS2, J85.3, U32.5, U33.1, U33.3
- net V_USB7: now also J43.VBUS1, J43.VBUS2, J47.6, U37.1, U37.3, U40.5; no longer J92.VBUS1, J92.VBUS2, J98.3, U37.5, U38.1, U38.3
- net V_USB8: now also J49.VBUS1, J49.VBUS2, J53.6, U42.1, U42.3, U45.5; no longer J105.VBUS1, J105.VBUS2, J111.3, U42.5, U43.1, U43.3
- net V_USB9: now also J55.VBUS1, J55.VBUS2, J59.6, U47.1, U47.3, U50.5; no longer J118.VBUS1, J118.VBUS2, J124.3, U47.5, U48.1, U48.3
- net WAKE_UP: now also J15.1; no longer J12.1
- net WAKE_UP1: now also J9.1, U9.15; no longer J25.1, U10.15
- net WAKE_UP10: now also J66.1, U54.15; no longer J142.1, U55.15
- net WAKE_UP11: now also J72.1, U59.15; no longer J155.1, U60.15
- net WAKE_UP2: now also J18.1, U14.15; no longer J38.1, U15.15
- net WAKE_UP3: now also J24.1, U19.15; no longer J51.1, U20.15
- net WAKE_UP4: now also J30.1, U24.15; no longer J64.1, U25.15
- net WAKE_UP5: now also J36.1, U29.15; no longer J77.1, U30.15
- net WAKE_UP6: now also J42.1, U34.15; no longer J90.1, U35.15
- net WAKE_UP7: now also J48.1, U39.15; no longer J103.1, U40.15
- net WAKE_UP8: now also J54.1, U44.15; no longer J116.1, U45.15
- net WAKE_UP9: now also J60.1, U49.15; no longer J129.1, U50.15
- net XM125_GPIO0: now also J15.9; no longer J8.1
- net XM125_GPIO1: now also J15.10; no longer J8.2
- net XM125_GPIO10: now also J36.10, U29.25; no longer J75.2, U30.25
- net XM125_GPIO11: now also J36.9, U29.24; no longer J75.1, U30.24
- net XM125_GPIO12: now also J42.10, U34.25; no longer J88.2, U35.25
- net XM125_GPIO13: now also J42.9, U34.24; no longer J88.1, U35.24
- net XM125_GPIO14: now also J48.10, U39.25; no longer J101.2, U40.25
- net XM125_GPIO15: now also J48.9, U39.24; no longer J101.1, U40.24
- net XM125_GPIO16: now also J54.10, U44.25; no longer J114.2, U45.25
- net XM125_GPIO17: now also J54.9, U44.24; no longer J114.1, U45.24
- net XM125_GPIO18: now also J60.10, U49.25; no longer J127.2, U50.25
- net XM125_GPIO19: now also J60.9, U49.24; no longer J127.1, U50.24
- net XM125_GPIO2: now also J9.10, U9.25; no longer J23.2, U10.25
- net XM125_GPIO2/BOOT0: now also J15.11; no longer J8.3
- net XM125_GPIO2/BOOT1: now also J9.11, U9.26; no longer J23.3, U10.26
- net XM125_GPIO2/BOOT10: now also J66.11, U54.26; no longer J140.3, U55.26
- net XM125_GPIO2/BOOT11: now also J72.11, U59.26; no longer J153.3, U60.26
- net XM125_GPIO2/BOOT2: now also J18.11, U14.26; no longer J36.3, U15.26
- net XM125_GPIO2/BOOT3: now also J24.11, U19.26; no longer J49.3, U20.26
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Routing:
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
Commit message: Final changes; reds ready for ordering!
Finished up Dryw's comments: see google doc for more information on specific changes made; panelized files updated and ready for ordering
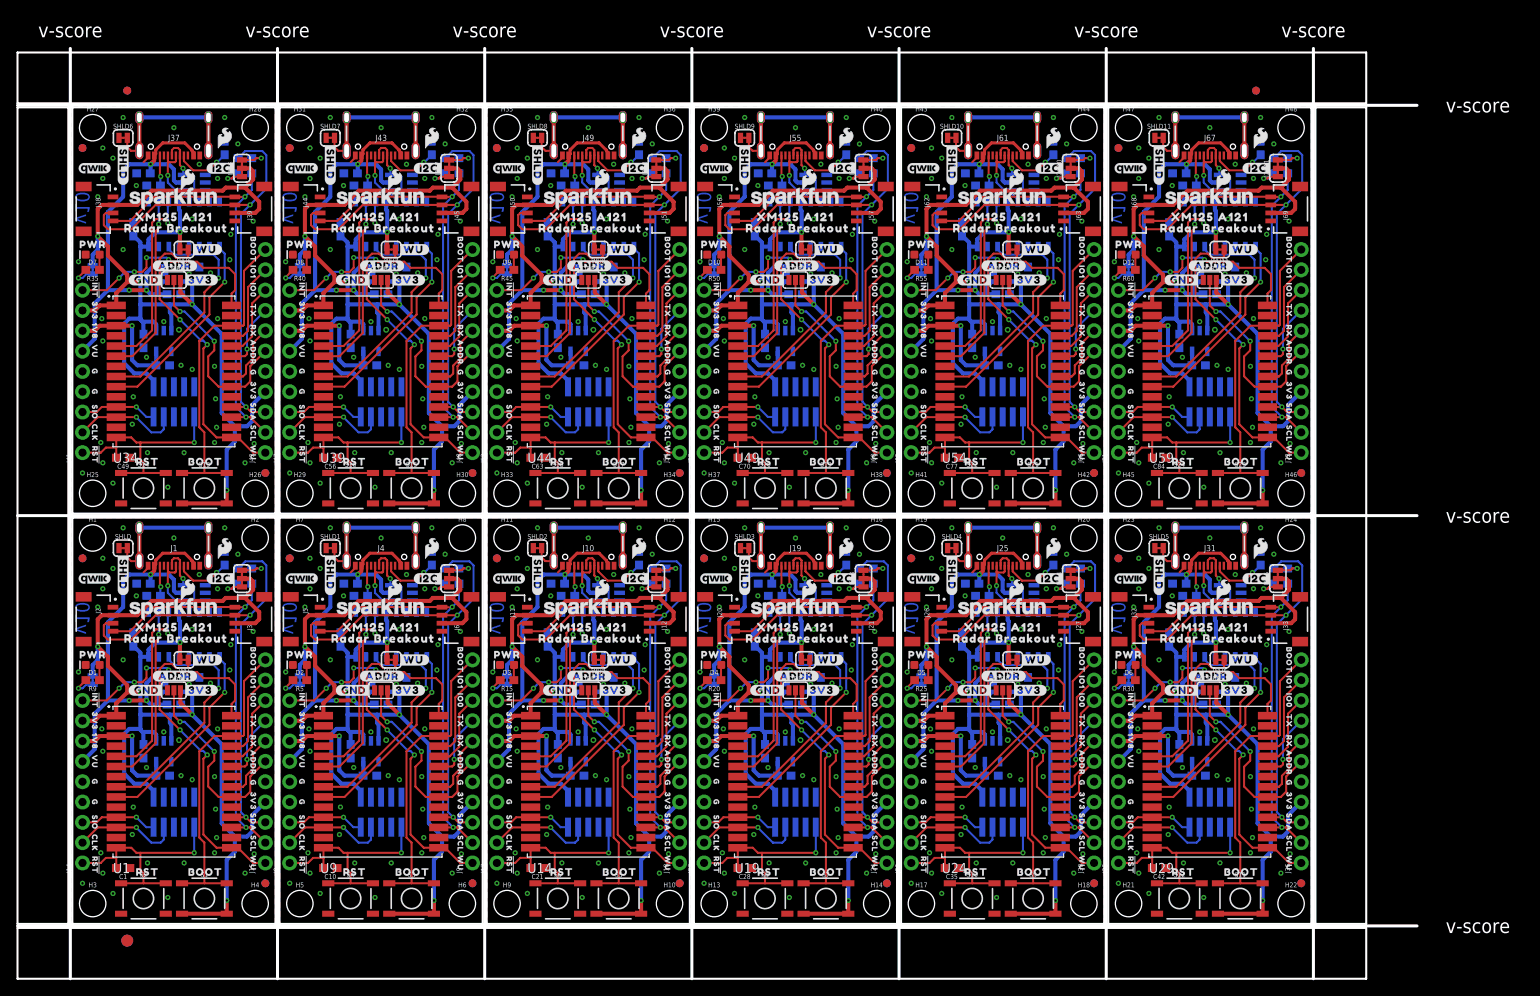
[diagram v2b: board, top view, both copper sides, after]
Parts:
- U$100, U$154, U$208, U$262, U$316, U$370, U$424, U$478, U$532, U$586, U$640: device output:#DEBUG_TX#10 -> output:#I2C_ADDR#12
- U$101, U$155, U$209, U$263, U$317, U$371, U$425, U$479, U$533, U$587, U$641: device output:#DEBUG_RX#11 -> output:#WAKE_UP#12
- U$102, U$156, U$210, U$264, U$318, U$372, U$426, U$480, U$534, U$588, U$642: device output:#I2C_ADDR#12 -> output:##RESET#13
- U$103, U$157, U$211, U$265, U$319, U$373, U$427, U$481, U$535, U$589, U$643: device output:#WAKE_UP#12 -> output:#WU#14
- U$104, U$158, U$212, U$266, U$320, U$374, U$428, U$482, U$536, U$590, U$644: device output:##RESET#13 -> output:#ADDR#16
- U$105, U$159, U$213, U$267, U$321, U$375, U$429, U$483, U$537, U$591, U$645: device output:#WU#14 -> output:#3V3#17
- U$106, U$160, U$214, U$268, U$322, U$376, U$430, U$484, U$538, U$592, U$646: device output:#ADDR#16 -> output:#GND#17
- U$107, U$161, U$215, U$269, U$323, U$377, U$431, U$485, U$539, U$593, U$647: device output:#3V3#17 -> output:#DEBUG_TX#18
- U$108, U$162, U$216, U$270, U$324, U$378, U$432, U$486, U$540, U$594, U$648: device output:#GND#17 -> output:#DEBUG_RX#19
- U$28: device output:#DEBUG_TX#10 -> output:#DEBUG_RX#19
- U$37: device output:#DEBUG_RX#11 -> output:BOOT21630063003532
- U$51: device output:BOOT21630063003532 -> output:#DEBUG_TX#18
- moved U$51 30.5 mm to (18.7, 25.4), flipped to the bottom
- moved U$37 28.9 mm to (42.5, 6.48), flipped to the top
- moved U$373 25.5 mm to (16.8, 84.3), flipped to the top
- moved U$427 25.5 mm to (42.7, 84.3), flipped to the top
- moved U$481 25.5 mm to (68.6, 84.3), flipped to the top
- moved U$535 25.5 mm to (94.5, 84.3), flipped to the top
- moved U$589 25.5 mm to (120.4, 84.3), flipped to the top
- moved U$643 25.5 mm to (146.3, 84.3), flipped to the top
- moved U$103 25.5 mm to (42.7, 33.0), flipped to the top
- moved U$157 25.5 mm to (68.6, 33.0), flipped to the top
- moved U$211 25.5 mm to (94.5, 33.0), flipped to the top
- moved U$265 25.5 mm to (120.4, 33.0), flipped to the top
- moved U$319 25.5 mm to (146.3, 33.0), flipped to the top
- moved U$374 24.7 mm to (12.8, 82.3), flipped to the top
- moved U$428 24.7 mm to (38.7, 82.3), flipped to the top
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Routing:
- net GND9: vias 40 -> 42
- net GND8: vias 40 -> 42
- net GND7: vias 40 -> 42
- net GND6: vias 40 -> 42
- net GND5: vias 40 -> 42
- net GND4: vias 40 -> 42
- net GND3: vias 40 -> 42
- net GND2: vias 40 -> 42
- net GND11: vias 40 -> 42
- net GND10: vias 40 -> 42
- net GND1: vias 40 -> 42
- net GND: vias 40 -> 42
